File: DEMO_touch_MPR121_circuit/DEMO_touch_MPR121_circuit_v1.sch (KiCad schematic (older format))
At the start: 16 parts, among them J1 Conn_01x10_Male, Q1 IPP060N06N, Q2 IPP060N06N, Q3 IPP060N06N, U1 ARDUINO_R3_ICSP, U2 MPR121_Arduino_shield, U4 VREG_board_MAKERFACTORY

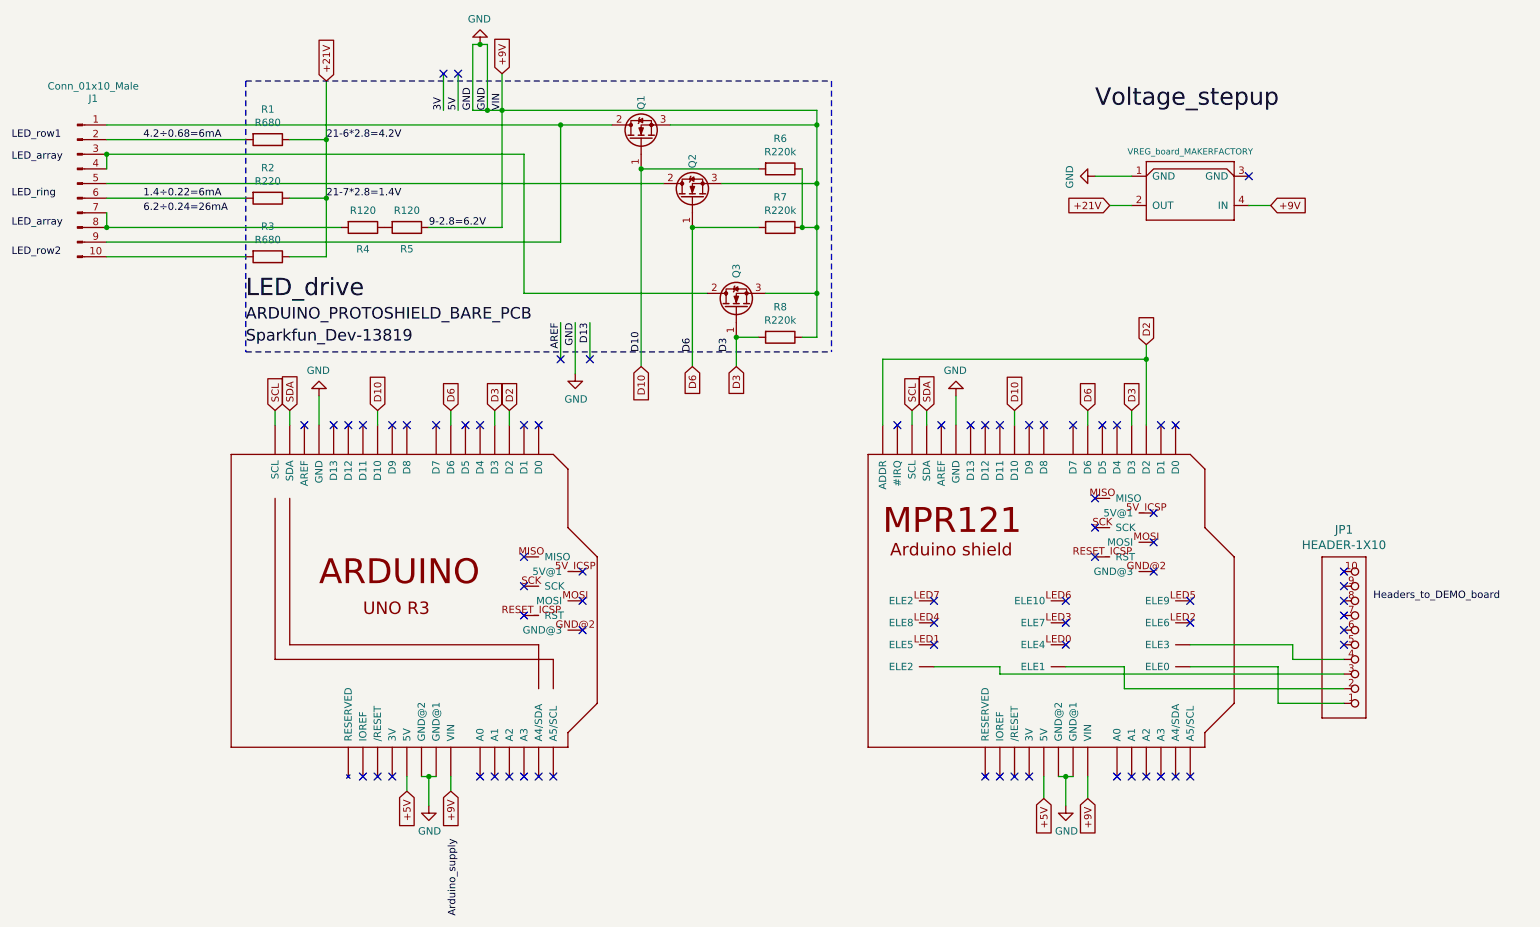
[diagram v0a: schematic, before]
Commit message: Circuit schematics update + LED power test sketch added
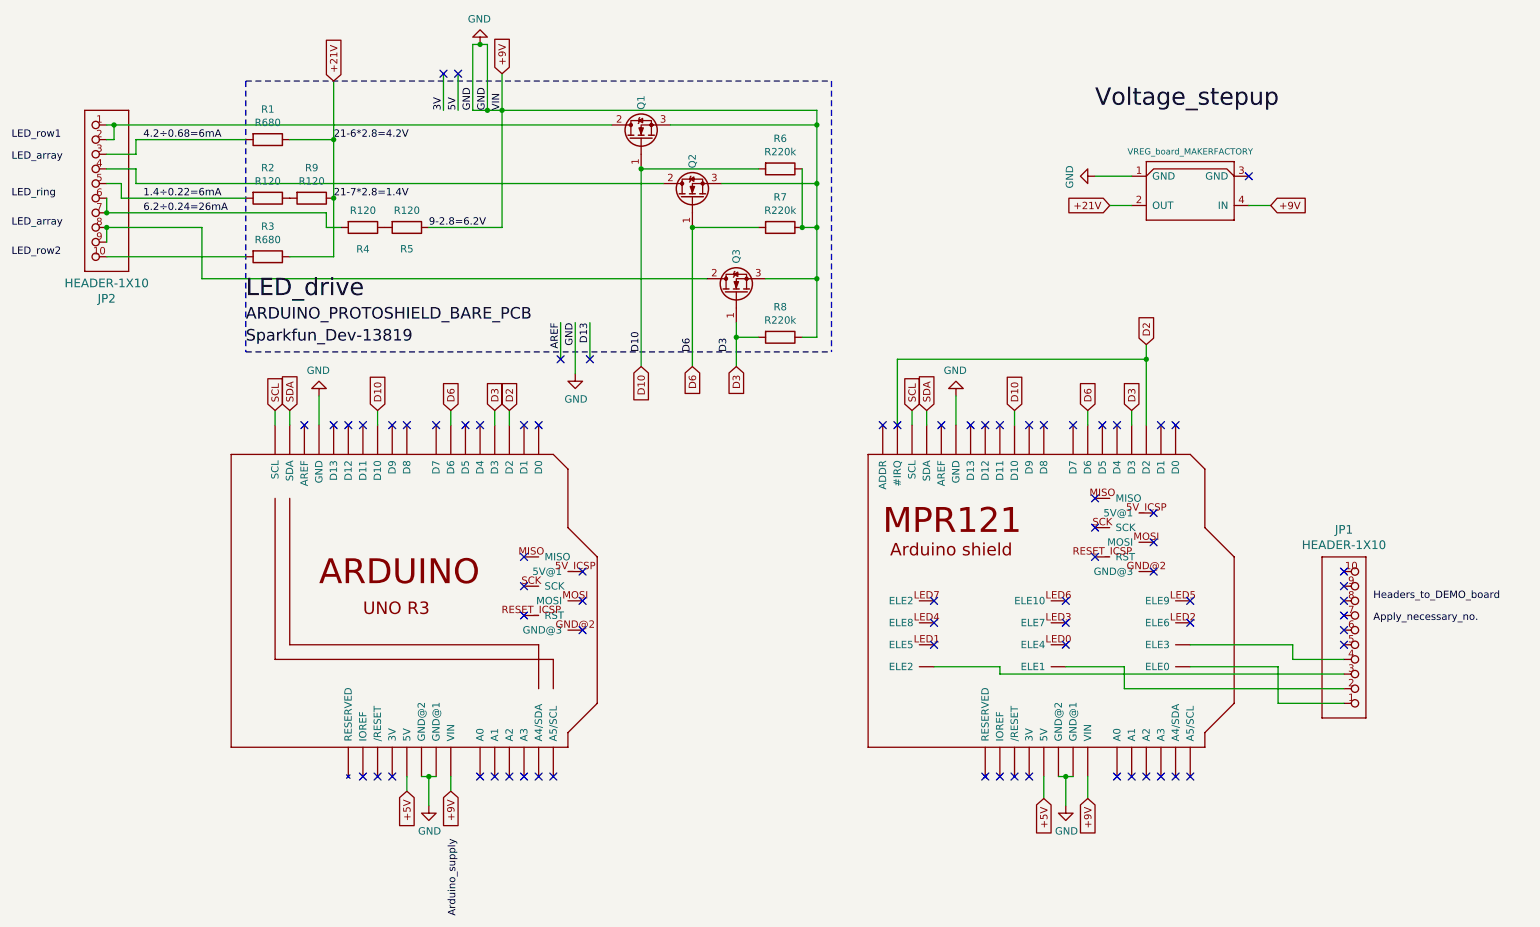
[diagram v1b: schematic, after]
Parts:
- removed J1: Conn_01x10_Male, symbol Connector:Conn_01x10_Male
- added JP2: HEADER-1X10, symbol Adafruit_MPR121_Capacitive_Touch_Shield-eagle-import:HEADER-1X10
- added R9: R120, lead wire, symbol Device:R
- R1, R3, R4, R5, R6, R7, R8: footprint (none) -> lead wire
- R2: value R220 -> R120; footprint (none) -> lead wire
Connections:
- net +21V: now also R9.1; no longer R2.1
- net 1.4÷0.22=6mA: now also JP2.5
- net 4.2÷0.68=6mA: now also JP2.3
- net 6.2÷0.24=26mA: now also R4.2, JP2.6, JP2.7
- net at Q1.2 (D): now also JP2.1, JP2.2
- net at Q2.2 (D): now also JP2.4
- net at Q3.2 (D): now also JP2.8, JP2.9
- net at R3.2: now also JP2.10
- new net: R2.1, R9.2
- no-connect marks 73 -> 74
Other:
- moved on the sheet: Q3
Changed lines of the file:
@@
 encoding utf-8
 Sheet 1 1
-Title ""
-Date ""
-Rev ""
-Comp ""
-Comment1 ""
-Comment2 ""
-Comment3 ""
+Title "Support electronics for row LED switching and capacitive sens."
+Date "01/11/2021 (mm/dd/yyyy)"
+Rev "v1"
+Comp "IZM Fraunhofer"
+Comment1 "v0: LED switching schematics"
+Comment2 "v0.1: + cap. sensing, and all neccessary hardware included"
+Comment3 "v1: LED power pins reordered for easier assembly; R2 value changed, R9 added"
 Comment4 ""
 $EndDescr
-Text GLabel 2950 1200 1    50   Input ~ 0
+Text GLabel 3000 1200 1    50   Input ~ 0
 +21V
-$Comp
-L Transistor_FET:IPP060N06N Q2
-U 1 1 5F4C3589
-P 5450 2000
-F 0 "Q2" H 5654 2000 50  0000 L CNN
-F 1 "IPP060N06N" H 5655 1955 50  0001 L CNN
-F 2 "Package_TO_SOT_THT:TO-220-3_Vertical" H 5700 1925 50  0001 L CIN
-F 3 "https://www.infineon.com/dgdl/Infineon-IPP060N06N-DS-v02_02-en.pdf?fileId=db3a30433727a44301372c06d9d7498a" H 5450 2000 50  0001 L CNN
-	1    5450 2000
-	0    -1   -1   0
-$EndComp
 $Comp
 L Device:R R1
@@
 F 0 "R1" V 2343 1600 50  0000 C CNN
 F 1 "R680" V 2434 1600 50  0000 C CNN
-F 2 "" V 2480 1600 50  0001 C CNN
+F 2 "lead wire" V 2480 1600 50  0001 C CNN
 F 3 "~" H 2550 1600 50  0001 C CNN
 	1    2550 1600
 	0    1    1    0
 $EndComp
-$Comp
-L Connector:Conn_01x10_Male J1
-U 1 1 5F4D07C0
-P 1250 1900
-F 0 "J1" H 1358 2481 50  0000 C CNN
-F 1 "Conn_01x10_Male" H 1358 2565 50  0000 C CNN
-F 2 "" H 1250 1900 50  0001 C CNN
-F 3 "~" H 1250 1900 50  0001 C CNN
-	1    1250 1900
-	1    0    0    -1
-$EndComp
-Wire Wire Line
-	1450 1700 1450 1800
-Wire Wire Line
-	1450 2200 1450 2100
-Wire Wire Line
-	2700 1600 2950 1600
 $Comp
 L Device:R R2
@@
 P 2550 2000
 F 0 "R2" V 2343 2000 50  0000 C CNN
-F 1 "R220" V 2434 2000 50  0000 C CNN
-F 2 "" V 2480 2000 50  0001 C CNN
+F 1 "R120" V 2434 2000 50  0000 C CNN
+F 2 "lead wire" V 2480 2000 50  0001 C CNN
 F 3 "~" H 2550 2000 50  0001 C CNN
 	1    2550 2000
 	0    1    1    0
 $EndComp
-Wire Wire Line
-	2700 2000 2950 2000
-Wire Wire Line
-	2700 2400 2950 2400
 $Comp
 L Device:R R3
@@
 F 0 "R3" V 2343 2400 50  0000 C CNN
 F 1 "R680" V 2434 2400 50  0000 C CNN
-F 2 "" V 2480 2400 50  0001 C CNN
+F 2 "lead wire" V 2480 2400 50  0001 C CNN
 F 3 "~" H 2550 2400 50  0001 C CNN
 	1    2550 2400
@@
 L Transistor_FET:IPP060N06N Q3
 U 1 1 5F4C5F7E
-P 5750 2750
-F 0 "Q3" H 5954 2750 50  0000 L CNN
-F 1 "IPP060N06N" H 5955 2705 50  0001 L CNN
-F 2 "Package_TO_SOT_THT:TO-220-3_Vertical" H 6000 2675 50  0001 L CIN
-F 3 "https://www.infineon.com/dgdl/Infineon-IPP060N06N-DS-v02_02-en.pdf?fileId=db3a30433727a44301372c06d9d7498a" H 5750 2750 50  0001 L CNN
-	1    5750 2750
+P 5750 2650
+F 0 "Q3" H 5954 2650 50  0000 L CNN
+F 1 "IPP060N06N" H 5955 2605 50  0001 L CNN
+F 2 "Package_TO_SOT_THT:TO-220-3_Vertical" H 6000 2575 50  0001 L CIN
+F 3 "https://www.infineon.com/dgdl/Infineon-IPP060N06N-DS-v02_02-en.pdf?fileId=db3a30433727a44301372c06d9d7498a" H 5750 2650 50  0001 L CNN
+	1    5750 2650
 	0    -1   -1   0
 $EndComp
-Wire Wire Line
-	4300 1700 4300 2650
-Wire Wire Line
-	4300 2650 5550 2650
-Connection ~ 1450 1700
-Wire Wire Line
-	5650 1900 6300 1900
 Connection ~ 6300 1900
-Wire Wire Line
-	5950 2650 6300 2650
 Text GLabel 5100 3150 3    50   Input ~ 0
 D10
@@
 F 0 "R6" V 5843 1800 50  0000 C CNN
 F 1 "R220k" V 5934 1800 50  0000 C CNN
-F 2 "" V 5980 1800 50  0001 C CNN
+F 2 "lead wire" V 5980 1800 50  0001 C CNN
 F 3 "~" H 6050 1800 50  0001 C CNN
 	1    6050 1800
@@
 F 0 "R7" V 5843 2200 50  0000 C CNN
 F 1 "R220k" V 5934 2200 50  0000 C CNN
-F 2 "" V 5980 2200 50  0001 C CNN
+F 2 "lead wire" V 5980 2200 50  0001 C CNN
 F 3 "~" H 6050 2200 50  0001 C CNN
 	1    6050 2200
@@
 F 0 "R8" V 5843 2950 50  0000 C CNN
 F 1 "R220k" V 5934 2950 50  0000 C CNN
-F 2 "" V 5980 2950 50  0001 C CNN
+F 2 "lead wire" V 5980 2950 50  0001 C CNN
 F 3 "~" H 6050 2950 50  0001 C CNN
 	1    6050 2950
@@
 Wire Wire Line
 	6200 2950 6300 2950
-Wire Wire Line
-	6300 2950 6300 2650
-Wire Wire Line
-	5900 2200 5450 2200
 Wire Wire Line
 	5750 2950 5900 2950
 Text GLabel 5750 3150 3    50   Input ~ 0
 D3
-Connection ~ 5750 2950
-Wire Wire Line
-	4550 2300 4550 1500
-Connection ~ 6300 2650
 Wire Wire Line
 	6300 1500 6300 1900
@@
 	6200 2200 6300 2200
 Wire Wire Line
-	6300 2200 6300 2650
+	6300 2200 6300 2550
 Connection ~ 6200 2200
 Text Label 1700 2100 0    50   ~ 0
@@
 	1450 2400 2400 2400
 Wire Wire Line
-	1450 2000 2400 2000
-Wire Wire Line
-	1450 1600 2400 1600
+	1450 1600 1500 1600
 Text Label 1700 1600 0    50   ~ 0
 4.2÷0.68=6mA
-Text Label 2950 1600 0    50   ~ 0
+Text Label 3000 1600 0    50   ~ 0
 21-6*2.8=4.2V
 Text Label 1700 2000 0    50   ~ 0
 1.4÷0.22=6mA
 Wire Wire Line
-	2950 1200 2950 1600
-Connection ~ 2950 1600
-Wire Wire Line
-	2950 1600 2950 2000
-Connection ~ 2950 2000
-Wire Wire Line
-	2950 2000 2950 2400
-Wire Wire Line
-	1450 1500 4550 1500
-Connection ~ 4550 1500
-Wire Wire Line
-	1450 2300 4550 2300
-Wire Wire Line
-	1450 1900 5250 1900
-Wire Wire Line
-	1450 1700 4300 1700
-Wire Wire Line
-	1450 2200 3050 2200
-Text Label 2950 2000 0    50   ~ 0
+	3000 1200 3000 1600
+Wire Wire Line
+	3000 1600 3000 2000
+Connection ~ 3000 2000
+Wire Wire Line
+	3000 2000 3000 2400
+Wire Wire Line
+	1450 1500 1500 1500
+Wire Wire Line
+	1450 1700 1650 1700
+Text Label 3000 2000 0    50   ~ 0
 21-7*2.8=1.4V
-Connection ~ 1450 2200
 $Comp
 L Device:R R4
@@
 F 0 "R4" V 3348 2200 50  0000 C CNN
 F 1 "R120" V 3084 2200 50  0000 C CNN
-F 2 "" V 3130 2200 50  0001 C CNN
+F 2 "lead wire" V 3130 2200 50  0001 C CNN
 F 3 "~" H 3200 2200 50  0001 C CNN
 	1    3200 2200
@@
 F 0 "R5" V 3647 2200 50  0000 C CNN
 F 1 "R120" V 3384 2200 50  0000 C CNN
-F 2 "" V 3430 2200 50  0001 C CNN
+F 2 "lead wire" V 3430 2200 50  0001 C CNN
 F 3 "~" H 3500 2200 50  0001 C CNN
 	1    3500 2200
@@
 F 1 "HEADER-1X10" H 9900 4369 59  0000 C CNN
 F 2 "" H 10000 5050 118 0001 C CNN
-F 3 "" H 10000 5050 118 0001 C CNN
+F 3 "~" H 10000 5050 118 0001 C CNN
 	1    10000 5050
 	1    0    0    1
@@
 	5750 3150 5750 2950
 Wire Wire Line
-	5450 2200 5450 3150
-Connection ~ 5450 2200
-Wire Wire Line
 	5300 1500 6300 1500
-Wire Wire Line
-	4550 1500 4900 1500
-Wire Wire Line
-	5100 1800 5900 1800
 $Comp
 L Transistor_FET:IPP060N06N Q1
@@
 Wire Wire Line
 	8550 3550 8550 3100
-Wire Wire Line
-	6750 3550 6750 3100
-Wire Wire Line
-	6750 3100 8550 3100
 Connection ~ 8550 3100
 Wire Wire Line
 	8550 3100 8550 3000
+Wire Wire Line
+	6850 3550 6850 3100
+Wire Wire Line
+	6850 3100 8550 3100
+NoConn ~ 6750 3550
+$Comp
+L Adafruit_MPR121_Capacitive_Touch_Shield-eagle-import:HEADER-1X10 JP2
+U 1 1 5FFD09A4
+P 1350 1900
+F 0 "JP2" H 1250 1114 59  0000 C CNN
+F 1 "HEADER-1X10" H 1250 1219 59  0000 C CNN
+F 2 "" H 1350 1900 118 0001 C CNN
+F 3 "~" H 1350 1900 118 0001 C CNN
+	1    1350 1900
+	-1   0    0    -1
+$EndComp
+Text Label 10100 4900 0    50   ~ 0
+Apply_necessary_no.
+Wire Wire Line
+	1500 1600 1500 1500
+Connection ~ 1500 1500
+Wire Wire Line
+	1650 1700 1650 1600
+Wire Wire Line
+	1650 1600 2400 1600
+Wire Wire Line
+	1650 1800 1450 1800
+Wire Wire Line
+	5100 1800 5900 1800
+Wire Wire Line
+	5650 1900 6300 1900
+Connection ~ 5450 2200
+Wire Wire Line
+	5450 2200 5450 3150
+Wire Wire Line
+	5900 2200 5450 2200
+Wire Wire Line
+	1650 1900 1650 1800
+$Comp
+L Transistor_FET:IPP060N06N Q2
+U 1 1 5F4C3589
+P 5450 2000
+F 0 "Q2" H 5654 2000 50  0000 L CNN
+F 1 "IPP060N06N" H 5655 1955 50  0001 L CNN
+F 2 "Package_TO_SOT_THT:TO-220-3_Vertical" H 5700 1925 50  0001 L CIN
+F 3 "https://www.infineon.com/dgdl/Infineon-IPP060N06N-DS-v02_02-en.pdf?fileId=db3a30433727a44301372c06d9d7498a" H 5450 2000 50  0001 L CNN
+	1    5450 2000
+	0    -1   -1   0
+$EndComp
+Wire Wire Line
+	1650 1900 5250 1900
+$Comp
+L Device:R R9
+U 1 1 5FFE115B
+P 2850 2000
+F 0 "R9" V 2643 2000 50  0000 C CNN
+F 1 "R120" V 2734 2000 50  0000 C CNN
+F 2 "lead wire" V 2780 2000 50  0001 C CNN
+F 3 "~" H 2850 2000 50  0001 C CNN
+	1    2850 2000
+	0    1    1    0
+$EndComp
+Connection ~ 3000 1600
+Wire Wire Line
+	2700 2400 3000 2400
+Wire Wire Line
+	2700 1600 3000 1600
+Wire Wire Line
+	1550 2000 1550 1900
+Wire Wire Line
+	1550 1900 1450 1900
+Wire Wire Line
+	1550 2000 2400 2000
+Wire Wire Line
+	1500 1500 4900 1500
+Wire Wire Line
+	1450 2000 1450 2100
+Wire Wire Line
+	1450 2100 2950 2100
+Wire Wire Line
+	2950 2100 2950 2200
+Connection ~ 1450 2100
+Wire Wire Line
+	2950 2200 3050 2200
+Wire Wire Line
+	1450 2200 1450 2300
+Wire Wire Line
+	1450 2200 2100 2200
+Wire Wire Line
+	2100 2200 2100 2550
+Connection ~ 1450 2200
+Wire Wire Line
+	2100 2550 5550 2550
+Wire Wire Line
+	5750 2850 5750 2950
+Connection ~ 5750 2950
+Wire Wire Line
+	5950 2550 6300 2550
+Connection ~ 6300 2550
+Wire Wire Line
+	6300 2550 6300 2950
 $EndSCHEMATC
